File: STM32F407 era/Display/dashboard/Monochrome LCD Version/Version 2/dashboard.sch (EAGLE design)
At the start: 93 parts, among them IC2 74HC14D, IC3 74HC14D, U1 CAT4238TD-GT3

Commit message: minor updates to power circuitry
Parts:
- removed D3: MBRS130LT3, diode:MBRS130LT3
- added D2: (no value), diode:SCHOTTKY-DIODESMC
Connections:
- net GND: now also D2.A; no longer D3.A
- net N$6: now also D2.C; no longer D3.C
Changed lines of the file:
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@@
 <part name="L2" library="SparkFun-Passives" deviceset="INDUCTOR" device="PWR" value="MSS1583-683MED"/>
 <part name="U$23" library="microbuilder" deviceset="3.3V" device=""/>
-<part name="D3" library="diode" deviceset="MBRS130LT3" device=""/>
 <part name="C25" library="rcl" deviceset="CPOL-EU" device="153CLV-1012" value="470u"/>
 <part name="C26" library="rcl" deviceset="CPOL-EU" device="153CLV-1012" value="220u"/>
@@
 <part name="U$72" library="microbuilder" deviceset="GND" device=""/>
 <part name="PTC1" library="microbuilder" deviceset="PTC" device="1812"/>
+<part name="D2" library="diode" deviceset="SCHOTTKY-DIODE" device="SMC"/>
 </parts>
 <sheets>
@@
 <instance part="L2" gate="G$1" x="73.66" y="-43.18" rot="R90"/>
 <instance part="U$23" gate="G$1" x="83.82" y="-38.1"/>
-<instance part="D3" gate="G$1" x="63.5" y="-58.42" rot="R90"/>
 <instance part="C25" gate="G$1" x="25.4" y="-53.34" rot="MR0"/>
 <instance part="C26" gate="G$1" x="83.82" y="-53.34" rot="MR0"/>
@@
 <instance part="U$72" gate="G$1" x="-182.88" y="-124.46"/>
 <instance part="PTC1" gate="G$1" x="25.4" y="-35.56" rot="R270"/>
+<instance part="D2" gate="G$1" x="63.5" y="-58.42" rot="R90"/>
 </instances>
 <busses>
@@
 <pinref part="U$18" gate="G$1" pin="GND"/>
 <wire x1="63.5" y1="-63.5" x2="63.5" y2="-60.96" width="0.1524" layer="91"/>
-<pinref part="D3" gate="G$1" pin="A"/>
+<pinref part="D2" gate="G$1" pin="A"/>
 </segment>
 <segment>
@@
 <junction x="63.5" y="-43.18"/>
 <pinref part="L2" gate="G$1" pin="1"/>
-<pinref part="D3" gate="G$1" pin="C"/>
-</segment>
-</net>
+<pinref part="D2" gate="G$1" pin="C"/>
+</segment>
+</net>

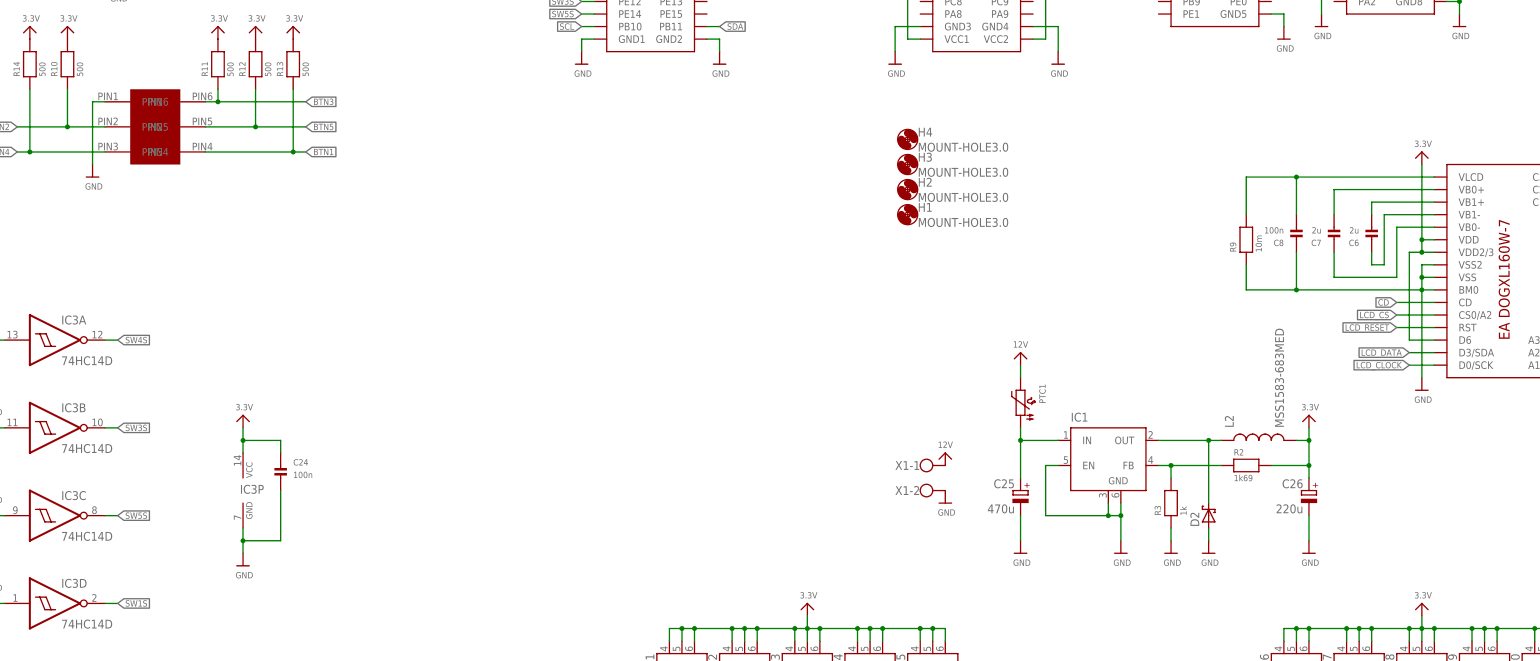
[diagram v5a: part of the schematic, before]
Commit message: added testpoints to power rails and coms, and created new Gerbers for PCB order
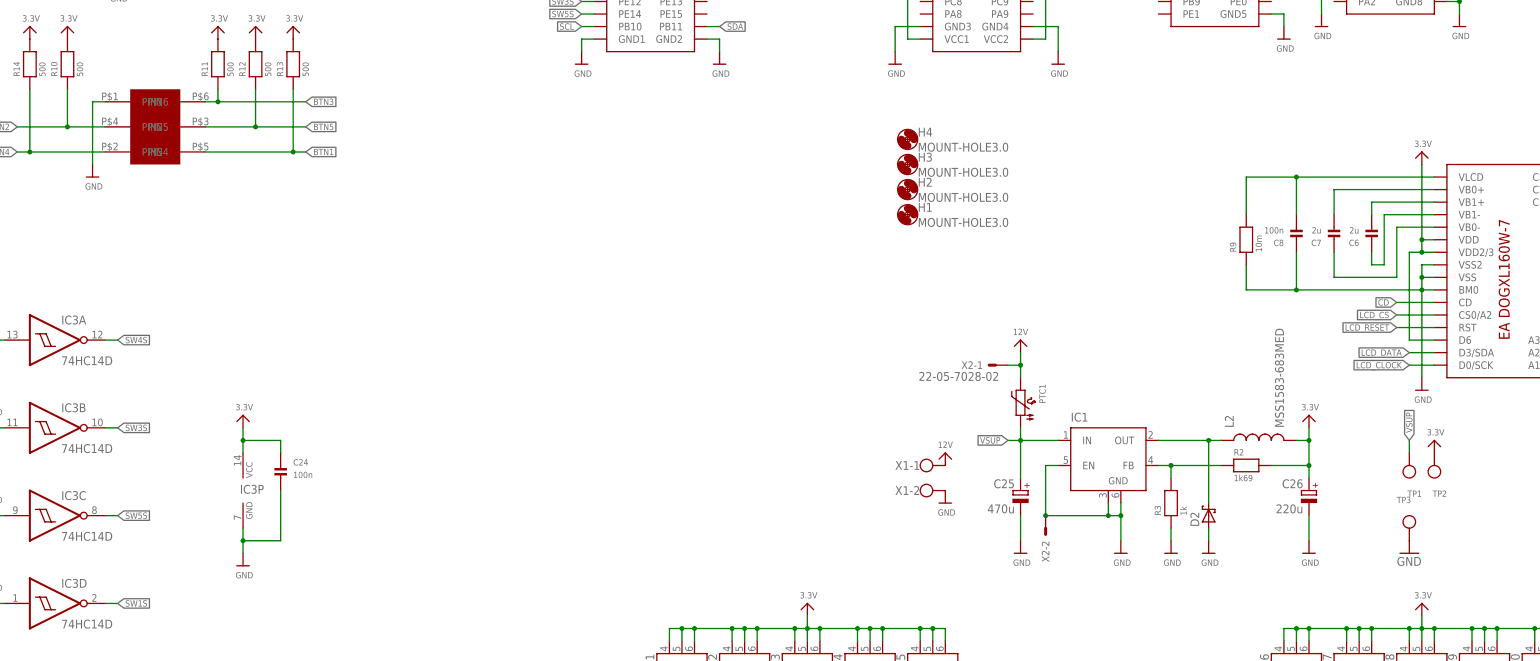
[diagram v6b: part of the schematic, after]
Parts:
- added TP1, TP2, TP3: (no value), microbuilder:TESTPOINT
- added X2: 22-05-7028-02, con-molex:22-05-7028-02
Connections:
- removed net N$77: C25.+, IC1.IN, PTC1.1
- new net VSUP: C25.+, IC1.IN, PTC1.1, TP1.P$1
- net 12V: now also X2-1.S
- net 3.3V: now also TP2.P$1
- net GND: now also TP3.P$1, X2-2.S
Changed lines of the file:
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@@
 <layer number="54" name="bGND_GNDA" color="1" fill="9" visible="no" active="no"/>
 <layer number="56" name="wert" color="7" fill="1" visible="no" active="no"/>
+<layer number="57" name="tCAD" color="7" fill="1" visible="no" active="no"/>
+<layer number="59" name="tCarbon" color="7" fill="1" visible="no" active="no"/>
+<layer number="60" name="bCarbon" color="7" fill="1" visible="no" active="no"/>
+<layer number="90" name="Modules" color="7" fill="1" visible="yes" active="yes"/>
 <layer number="91" name="Nets" color="2" fill="1" visible="yes" active="yes"/>
 <layer number="92" name="Busses" color="1" fill="1" visible="yes" active="yes"/>
@@
 <layer number="97" name="Info" color="7" fill="1" visible="yes" active="yes"/>
 <layer number="98" name="Guide" color="6" fill="1" visible="yes" active="yes"/>
+<layer number="99" name="SpiceOrder" color="7" fill="1" visible="yes" active="yes"/>
 <layer number="100" name="Muster" color="7" fill="1" visible="no" active="no"/>
 <layer number="101" name="Patch_Top" color="12" fill="4" visible="yes" active="yes"/>
@@
 <layer number="111" name="MPL" color="7" fill="1" visible="yes" active="yes"/>
 <layer number="112" name="tSilk" color="7" fill="1" visible="yes" active="yes"/>
+<layer number="113" name="IDFDebug" color="7" fill="1" visible="yes" active="yes"/>
+<layer number="114" name="Badge_Outline" color="7" fill="1" visible="yes" active="yes"/>
+<layer number="115" name="ReferenceISLANDS" color="7" fill="1" visible="yes" active="yes"/>
 <layer number="116" name="Patch_BOT" color="9" fill="4" visible="yes" active="yes"/>
+<layer number="118" name="Rect_Pads" color="7" fill="1" visible="yes" active="yes"/>
 <layer number="121" name="_tsilk" color="7" fill="1" visible="yes" active="yes"/>
 <layer number="122" name="_bsilk" color="7" fill="1" visible="yes" active="yes"/>
+<layer number="123" name="tTestmark" color="7" fill="1" visible="yes" active="yes"/>
+<layer number="124" name="bTestmark" color="7" fill="1" visible="yes" active="yes"/>
 <layer number="125" name="_tNames" color="7" fill="1" visible="yes" active="yes"/>
 <layer number="126" name="_bNames" color="7" fill="1" visible="yes" active="yes"/>
 <layer number="127" name="_tValues" color="7" fill="1" visible="yes" active="yes"/>
 <layer number="128" name="_bValues" color="7" fill="1" visible="yes" active="yes"/>
+<layer number="129" name="Mask" color="7" fill="1" visible="yes" active="yes"/>
+<layer number="131" name="tAdjust" color="7" fill="1" visible="yes" active="yes"/>
+<layer number="132" name="bAdjust" color="7" fill="1" visible="yes" active="yes"/>
 <layer number="144" name="Drill_legend" color="7" fill="1" visible="yes" active="yes"/>
+<layer number="150" name="Notes" color="7" fill="1" visible="yes" active="yes"/>
 <layer number="151" name="HeatSink" color="7" fill="1" visible="yes" active="yes"/>
 <layer number="152" name="_bDocu" color="7" fill="1" visible="yes" active="yes"/>
+<layer number="153" name="FabDoc1" color="7" fill="1" visible="yes" active="yes"/>
+<layer number="154" name="FabDoc2" color="7" fill="1" visible="yes" active="yes"/>
+<layer number="155" name="FabDoc3" color="7" fill="1" visible="yes" active="yes"/>
 <layer number="199" name="Contour" color="7" fill="1" visible="yes" active="yes"/>
 <layer number="200" name="200bmp" color="1" fill="10" visible="yes" active="yes"/>
@@
 <layer number="223" name="223bmp" color="24" fill="1" visible="no" active="no"/>
 <layer number="224" name="224bmp" color="25" fill="1" visible="no" active="no"/>
+<layer number="225" name="225bmp" color="7" fill="1" visible="yes" active="yes"/>
+<layer number="226" name="226bmp" color="7" fill="1" visible="yes" active="yes"/>
+<layer number="227" name="227bmp" color="7" fill="1" visible="yes" active="yes"/>
+<layer number="228" name="228bmp" color="7" fill="1" visible="yes" active="yes"/>
+<layer number="229" name="229bmp" color="7" fill="1" visible="yes" active="yes"/>
+<layer number="230" name="230bmp" color="7" fill="1" visible="yes" active="yes"/>
+<layer number="231" name="231bmp" color="7" fill="1" visible="yes" active="yes"/>
+<layer number="232" name="Eagle3D_PG2" color="7" fill="1" visible="yes" active="yes"/>
+<layer number="233" name="Eagle3D_PG3" color="7" fill="1" visible="yes" active="yes"/>
 <layer number="248" name="Housing" color="7" fill="1" visible="yes" active="yes"/>
 <layer number="249" name="Edge" color="7" fill="1" visible="yes" active="yes"/>
@@
 <layer number="251" name="SMDround" color="12" fill="11" visible="no" active="no"/>
 <layer number="254" name="cooling" color="7" fill="1" visible="yes" active="yes"/>
+<layer number="255" name="routoute" color="7" fill="1" visible="yes" active="yes"/>
 </layers>
 <schematic xreflabel="%F%N/%S.%C%R" xrefpart="/%S.%C%R">
@@
 <part name="PTC1" library="microbuilder" deviceset="PTC" device="1812"/>
 <part name="D2" library="diode" deviceset="SCHOTTKY-DIODE" device="SMC"/>
+<part name="X2" library="con-molex" deviceset="22-?-02" device="05-7028">
+<attribute name="MF" value=""/>
+<attribute name="MPN" value=""/>
+<attribute name="OC_FARNELL" value="9731601"/>
+<attribute name="OC_NEWARK" value="unknown"/>
+</part>
+<part name="U$77" library="microbuilder" deviceset="3.3V" device=""/>
+<part name="GND26" library="supply1" deviceset="GND" device=""/>
+<part name="TP1" library="microbuilder" deviceset="TESTPOINT" device=""/>
+<part name="TP2" library="microbuilder" deviceset="TESTPOINT" device=""/>
+<part name="TP3" library="microbuilder" deviceset="TESTPOINT" device=""/>
 </parts>
 <sheets>
@@
 <instance part="R3" gate="G$1" x="55.88" y="-55.88" rot="R90"/>
 <instance part="U$19" gate="G$1" x="55.88" y="-66.04"/>
-<instance part="U$20" gate="G$1" x="25.4" y="-25.4"/>
+<instance part="U$20" gate="G$1" x="25.4" y="-22.86"/>
 <instance part="U$21" gate="G$1" x="25.4" y="-66.04"/>
 <instance part="U$22" gate="G$1" x="83.82" y="-66.04"/>
@@
 <instance part="PTC1" gate="G$1" x="25.4" y="-35.56" rot="R270"/>
 <instance part="D2" gate="G$1" x="63.5" y="-58.42" rot="R90"/>
+<instance part="X2" gate="-2" x="30.48" y="-60.96" rot="R270"/>
+<instance part="X2" gate="-1" x="20.32" y="-27.94" rot="R180"/>
+<instance part="U$77" gate="G$1" x="109.22" y="-43.18"/>
+<instance part="GND26" gate="1" x="104.14" y="-66.04"/>
+<instance part="TP1" gate="G$1" x="104.14" y="-45.72" rot="R180"/>
+<instance part="TP2" gate="G$1" x="109.22" y="-45.72" rot="R180"/>
+<instance part="TP3" gate="G$1" x="104.14" y="-63.5"/>
 </instances>
 <busses>
@@
 <wire x1="43.18" y1="-55.88" x2="43.18" y2="-58.42" width="0.1524" layer="91"/>
 <junction x="43.18" y="-58.42"/>
+<pinref part="X2" gate="-2" pin="S"/>
+<junction x="30.48" y="-58.42"/>
 </segment>
 <segment>
@@
 <pinref part="C4" gate="G$1" pin="P$1"/>
 <pinref part="U$72" gate="G$1" pin="GND"/>
+</segment>
+<segment>
+<pinref part="GND26" gate="1" pin="GND"/>
+<pinref part="TP3" gate="G$1" pin="P$1"/>
 </segment>
 </net>
@@
 <pinref part="C26" gate="G$1" pin="+"/>
 </segment>
+<segment>
+<pinref part="U$77" gate="G$1" pin="3.3V"/>
+<pinref part="TP2" gate="G$1" pin="P$1"/>
+</segment>
 </net>
 <net name="12V" class="0">
@@
 <pinref part="U$20" gate="G$1" pin="12V"/>
 <wire x1="25.4" y1="-30.48" x2="25.4" y2="-27.94" width="0.1524" layer="91"/>
+<pinref part="X2" gate="-1" pin="S"/>
+<wire x1="25.4" y1="-27.94" x2="25.4" y2="-25.4" width="0.1524" layer="91"/>
+<wire x1="22.86" y1="-27.94" x2="25.4" y2="-27.94" width="0.1524" layer="91"/>
+<junction x="25.4" y="-27.94"/>
 </segment>
 </net>
@@
 </segment>
 </net>
-<net name="N$77" class="0">
+<net name="VSUP" class="0">
+<segment>
+<pinref part="TP1" gate="G$1" pin="P$1"/>
+<wire x1="104.14" y1="-43.18" x2="104.14" y2="-45.72" width="0.1524" layer="91"/>
+<label x="104.14" y="-43.18" size="1.27" layer="95" rot="R90" xref="yes"/>
+</segment>
 <segment>
 <pinref part="IC1" gate="G$1" pin="IN"/>
@@
 <wire x1="25.4" y1="-40.64" x2="25.4" y2="-43.18" width="0.1524" layer="91"/>
 <junction x="25.4" y="-43.18"/>
-</segment>
-</net>
+<wire x1="22.86" y1="-43.18" x2="25.4" y2="-43.18" width="0.1524" layer="91"/>
+<label x="22.86" y="-43.18" size="1.27" layer="95" rot="R180" xref="yes"/>
+</segment>
+</net>
